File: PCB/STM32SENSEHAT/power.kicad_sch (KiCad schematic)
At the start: 23 parts, among them Q1 FS8205A, U1 MCP1700x-330xxTT, U11 AO3401A_C306862

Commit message: PCB draft
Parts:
- C10, C11, C15, C20, C21: footprint JLCfootprint:C0805 -> Capacitor_SMD:C_0805_2012Metric
- R36, R39, R4, R40, R5, R6: footprint JLCfootprint:R0805 -> Resistor_SMD:R_0805_2012Metric
- U2: value ~ -> DW01A
- U7: value ~ -> TP4056
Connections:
- net BATT+: now also D1.2 (A); no longer BT2.1 (+)
- net at C15.2, Q1.2, Q1.3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: now also BT2.2 (-); no longer D1.1 (K)
- new net: BT2.1 (+), D1.1 (K)
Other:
- moved on the sheet: BT2, R39

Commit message: Changed the footprint of cpacitors C10 and C11 to C_disc"
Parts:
- C10, C11: footprint Capacitor_SMD:C_0805_2012Metric -> Capacitor_THT:C_Disc_D5.0mm_W2.5mm_P5.00mm
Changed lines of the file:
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@@
       (effects (font (size 1.27 1.27)) (justify left))
     )
-    (property "Footprint" "Capacitor_SMD:C_0805_2012Metric" (at 300.99 124.46 0)
+    (property "Footprint" "Capacitor_THT:C_Disc_D5.0mm_W2.5mm_P5.00mm" (at 300.99 124.46 0)
       (effects (font (size 1.27 1.27)) hide)
     )
@@
       (effects (font (size 1.27 1.27)) (justify left))
     )
-    (property "Footprint" "Capacitor_SMD:C_0805_2012Metric" (at 271.78 121.92 0)
-      (effects (font (size 1.27 1.27)) hide)
-    )
+    (property "Footprint" "Capacitor_THT:C_Disc_D5.0mm_W2.5mm_P5.00mm" (at 271.78 121.92 0)
+      (effects (font (size 1.27 1.27)) hide)
+    )

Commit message: Update
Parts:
- C15: value 10nF -> 100nF
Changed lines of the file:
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@@
       (effects (font (size 1.27 1.27)) (justify left))
     )
-    (property "Value" "10nF" (at 107.95 165.7413 0)
+    (property "Value" "100nF" (at 107.95 165.7413 0)
       (effects (font (size 1.27 1.27)) (justify left))
     )

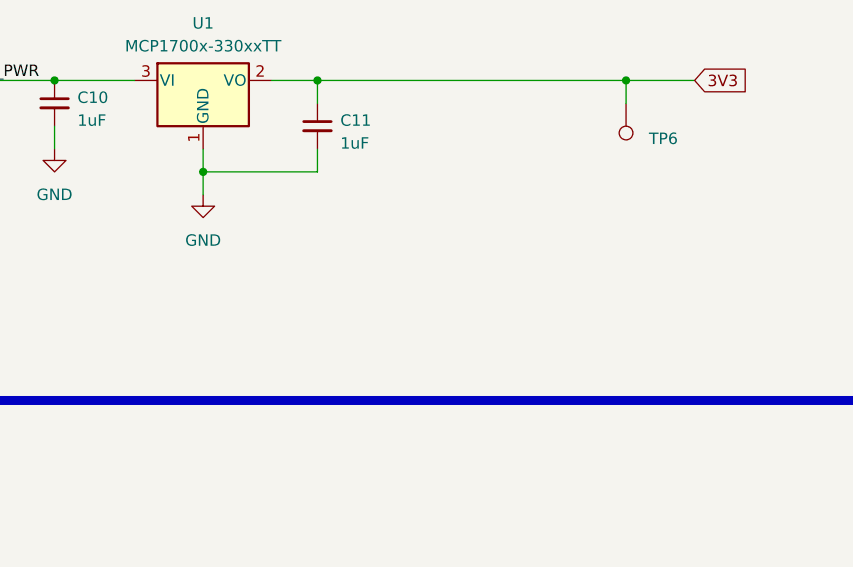
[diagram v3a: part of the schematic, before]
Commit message: Added a poer indicator LED and rectified NRST parastic capacitance
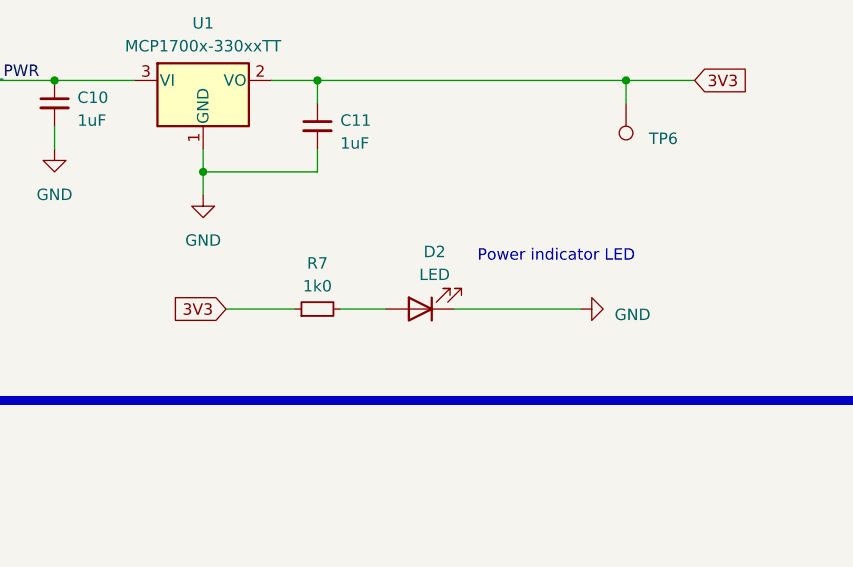
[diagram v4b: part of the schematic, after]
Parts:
- added D2: LED, LED_THT:LED_D5.0mm, symbol Device:LED
- added R7: 1k0, Resistor_SMD:R_0805_2012Metric, symbol Device:R_Small
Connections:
- net 3V3: now also R7.1
- net GND: now also D2.1 (K)
- new net: D2.2 (A), R7.2
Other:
- note added: "Power indicator LED"
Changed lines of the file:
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@@
+    (stroke (width 0) (type default))
+  )
+  (wire (pts (xy 316.23 144.78) (xy 330.2 144.78))
     (stroke (width 0) (type default))
   )
@@
     (stroke (width 0) (type default))
   )
+  (wire (pts (xy 290.83 144.78) (xy 298.45 144.78))
+    (stroke (width 0) (type default))
+  )
   (wire (pts (xy 144.78 92.71) (xy 203.2 92.71))
     (stroke (width 0) (type default))
@@
   )
   (wire (pts (xy 88.9 177.8) (xy 86.36 177.8))
+    (stroke (width 0) (type default))
+  )
+  (wire (pts (xy 303.53 144.78) (xy 308.61 144.78))
     (stroke (width 0) (type default))
   )
@@
     (effects (font (size 5 5) (thickness 0.5) bold) (justify left bottom))
   )
+  (text "Power indicator LED" (at 318.77 139.7 0)
+    (effects (font (size 1.27 1.27)) (justify left bottom))
+  )
   (text "BATTERY PROTECTION" (at 92.71 127 0)
     (effects (font (size 5 5) (thickness 0.5) bold) (justify left bottom))
@@
     )
   )
+  (global_label "3V3" (shape input) (at 290.83 144.78 180) (fields_autoplaced)
+    (effects (font (size 1.27 1.27)) (justify right))
+    (property "Intersheetrefs" "${INTERSHEET_REFS}" (at 284.4166 144.78 0)
+      (effects (font (size 1.27 1.27)) (justify right) hide)
+    )
+  )
   (global_label "5VUSB" (shape input) (at 152.4 139.7 90) (fields_autoplaced)
     (effects (font (size 1.27 1.27)) (justify left))
@@
     )
   )
+  (symbol (lib_id "Device:LED") (at 312.42 144.78 180) (unit 1)
+    (in_bom yes) (on_board yes) (dnp no) (fields_autoplaced)
+    (property "Reference" "D2" (at 314.0075 138.43 0)
+      (effects (font (size 1.27 1.27)))
+    )
+    (property "Value" "LED" (at 314.0075 140.97 0)
+      (effects (font (size 1.27 1.27)))
+    )
+    (property "Footprint" "LED_THT:LED_D5.0mm" (at 312.42 144.78 0)
+      (effects (font (size 1.27 1.27)) hide)
+    )
+    (property "Datasheet" "~" (at 312.42 144.78 0)
+      (effects (font (size 1.27 1.27)) hide)
+    )
+    (property "Basic" "" (at 312.42 144.78 0)
+      (effects (font (size 1.27 1.27)) hide)
+    )
+    (property "DNP" "" (at 312.42 144.78 0)
+      (effects (font (size 1.27 1.27)) hide)
+    )
+    (property "Extended" "" (at 312.42 144.78 0)
+      (effects (font (size 1.27 1.27)) hide)
+    )
+    (property "MOQ and Attrition" "" (at 312.42 144.78 0)
+      (effects (font (size 1.27 1.27)) hide)
+    )
+    (property "Price" "" (at 312.42 144.78 0)
+      (effects (font (size 1.27 1.27)) hide)
+    )
+    (pin "1")
+    (pin "2")
+    (instances
+      (project "STM32SENSEHAT"
+        (path "/e47212d5-bd6f-4bb8-9ec7-12aac08f34b5/e2c75964-4e94-4a3b-9ddf-38bb01f2971b"
+          (reference "D2") (unit 1)
+        )
+      )
+    )
+  )
   (symbol (lib_id "power:GND") (at 166.37 77.47 0) (unit 1)
     (in_bom yes) (on_board yes) (dnp no) (fields_autoplaced)
@@
         (path "/e47212d5-bd6f-4bb8-9ec7-12aac08f34b5/e2c75964-4e94-4a3b-9ddf-38bb01f2971b"
           (reference "R5") (unit 1)
+        )
+      )
+    )
+  )
+  (symbol (lib_id "Device:R_Small") (at 300.99 144.78 90) (unit 1)
+    (in_bom yes) (on_board yes) (dnp no) (fields_autoplaced)
+    (property "Reference" "R7" (at 300.99 139.7 90)
+      (effects (font (size 1.27 1.27)))
+    )
+    (property "Value" "1k0" (at 300.99 142.24 90)
+      (effects (font (size 1.27 1.27)))
+    )
+    (property "Footprint" "Resistor_SMD:R_0805_2012Metric" (at 300.99 144.78 0)
+      (effects (font (size 1.27 1.27)) hide)
+    )
+    (property "Datasheet" "~" (at 300.99 144.78 0)
+      (effects (font (size 1.27 1.27)) hide)
+    )
+    (property "Basic" "" (at 300.99 144.78 0)
+      (effects (font (size 1.27 1.27)) hide)
+    )
+    (property "DNP" "" (at 300.99 144.78 0)
+      (effects (font (size 1.27 1.27)) hide)
+    )
+    (property "Extended" "" (at 300.99 144.78 0)
+      (effects (font (size 1.27 1.27)) hide)
+    )
+    (property "MOQ and Attrition" "" (at 300.99 144.78 0)
+      (effects (font (size 1.27 1.27)) hide)
+    )
+    (property "Price" "" (at 300.99 144.78 0)
+      (effects (font (size 1.27 1.27)) hide)
+    )
+    (pin "1")
+    (pin "2")
+    (instances
+      (project "STM32SENSEHAT"
+        (path "/e47212d5-bd6f-4bb8-9ec7-12aac08f34b5/e2c75964-4e94-4a3b-9ddf-38bb01f2971b"
+          (reference "R7") (unit 1)
         )
       )
@@
         )
       )
+    )
+  )
+  (symbol (lib_id "power:GND") (at 330.2 144.78 90) (unit 1)
+    (in_bom yes) (on_board yes) (dnp no) (fields_autoplaced)
+    (property "Reference" "#PWR039" (at 336.55 144.78 0)
+      (effects (font (size 1.27 1.27)) hide)
+    )
+    (property "Value" "GND" (at 334.01 145.415 90)
+      (effects (font (size 1.27 1.27)) (justify right))
+    )
+    (property "Footprint" "" (at 330.2 144.78 0)
+      (effects (font (size 1.27 1.27)) hide)
+    )
+    (property "Datasheet" "" (at 330.2 144.78 0)
+      (effects (font (size 1.27 1.27)) hide)
+    )
+    (pin "1")
+    (instances
+      (project "STM32SENSEHAT"
+        (path "/e47212d5-bd6f-4bb8-9ec7-12aac08f34b5/e2c75964-4e94-4a3b-9ddf-38bb01f2971b"
+          (reference "#PWR039") (unit 1)
+        )
+      )

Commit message: Added Justin's Feedback
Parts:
- added R22: 1k0, Resistor_SMD:R_0805_2012Metric, symbol Device:R_Small
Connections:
- net 5VUSB: now also R22.1
- net at D4.2 (A), R40.2: no longer D5.2 (A)
- new net: D5.2 (A), R22.2
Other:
- moved on the sheet: D5, R40
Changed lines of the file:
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@@
   (junction (at 128.27 158.75) (diameter 0) (color 0 0 0 0)
   )
-  (junction (at 83.82 49.53) (diameter 0) (color 0 0 0 0)
-  )
   (junction (at 110.49 158.75) (diameter 0) (color 0 0 0 0)
   )
   (junction (at 67.31 191.77) (diameter 0) (color 0 0 0 0)
   )
+  (junction (at 74.93 49.53) (diameter 0) (color 0 0 0 0)
+  )
   (junction (at 165.1 144.78) (diameter 0) (color 0 0 0 0)
   )
@@
   (junction (at 152.4 144.78) (diameter 0) (color 0 0 0 0)
   )
-  (junction (at 83.82 55.88) (diameter 0) (color 0 0 0 0)
-  )
   (junction (at 144.78 92.71) (diameter 0) (color 0 0 0 0)
   )
@@
   )
   (junction (at 173.99 158.75) (diameter 0) (color 0 0 0 0)
+  )
+  (junction (at 88.9 49.53) (diameter 0) (color 0 0 0 0)
   )
   (junction (at 48.26 49.53) (diameter 0) (color 0 0 0 0)
@@
     (stroke (width 0) (type default))
   )
-  (wire (pts (xy 93.98 57.15) (xy 93.98 55.88))
+  (wire (pts (xy 88.9 57.15) (xy 88.9 55.88))
     (stroke (width 0) (type default))
   )
@@
     (stroke (width 0) (type default))
   )
-  (wire (pts (xy 83.82 55.88) (xy 74.93 55.88))
-    (stroke (width 0) (type default))
-  )
   (wire (pts (xy 335.28 119.38) (xy 335.28 121.92))
     (stroke (width 0) (type default))
@@
     (stroke (width 0) (type default))
   )
-  (wire (pts (xy 83.82 49.53) (xy 100.33 49.53))
-    (stroke (width 0) (type default))
-  )
   (wire (pts (xy 132.08 92.71) (xy 144.78 92.71))
     (stroke (width 0) (type default))
@@
     (stroke (width 0) (type default))
   )
+  (wire (pts (xy 74.93 49.53) (xy 88.9 49.53))
+    (stroke (width 0) (type default))
+  )
   (wire (pts (xy 271.78 127) (xy 271.78 124.46))
     (stroke (width 0) (type default))
@@
     (stroke (width 0) (type default))
   )
-  (wire (pts (xy 83.82 49.53) (xy 83.82 50.8))
+  (wire (pts (xy 74.93 49.53) (xy 74.93 50.8))
     (stroke (width 0) (type default))
   )
@@
     (stroke (width 0) (type default))
   )
-  (wire (pts (xy 93.98 55.88) (xy 83.82 55.88))
-    (stroke (width 0) (type default))
-  )
   (wire (pts (xy 128.27 184.15) (xy 128.27 191.77))
     (stroke (width 0) (type default))
@@
     (stroke (width 0) (type default))
   )
+  (wire (pts (xy 88.9 49.53) (xy 88.9 50.8))
+    (stroke (width 0) (type default))
+  )
   (wire (pts (xy 67.31 168.91) (xy 67.31 171.45))
     (stroke (width 0) (type default))
@@
     (stroke (width 0) (type default))
   )
-  (wire (pts (xy 93.98 64.77) (xy 93.98 66.04))
+  (wire (pts (xy 88.9 64.77) (xy 88.9 66.04))
     (stroke (width 0) (type default))
   )
@@
     (stroke (width 0) (type default))
   )
-  (wire (pts (xy 52.07 49.53) (xy 83.82 49.53))
+  (wire (pts (xy 52.07 49.53) (xy 74.93 49.53))
     (stroke (width 0) (type default))
   )
@@
     (stroke (width 0) (type default))
   )
-  (wire (pts (xy 93.98 66.04) (xy 107.95 66.04))
+  (wire (pts (xy 88.9 66.04) (xy 107.95 66.04))
     (stroke (width 0) (type default))
   )
   (wire (pts (xy 110.49 168.91) (xy 110.49 166.37))
+    (stroke (width 0) (type default))
+  )
+  (wire (pts (xy 88.9 49.53) (xy 100.33 49.53))
     (stroke (width 0) (type default))
   )
@@
     )
   )
+  (symbol (lib_id "Device:R_Small") (at 88.9 53.34 0) (unit 1)
+    (in_bom yes) (on_board yes) (dnp no) (fields_autoplaced)
+    (property "Reference" "R22" (at 91.44 52.705 0)
+      (effects (font (size 1.27 1.27)) (justify left))
+    )
+    (property "Value" "1k0" (at 91.44 55.245 0)
+      (effects (font (size 1.27 1.27)) (justify left))
+    )
+    (property "Footprint" "Resistor_SMD:R_0805_2012Metric" (at 88.9 53.34 0)
+      (effects (font (size 1.27 1.27)) hide)
+    )
+    (property "Datasheet" "~" (at 88.9 53.34 0)
+      (effects (font (size 1.27 1.27)) hide)
+    )
+    (property "Basic" "" (at 88.9 53.34 0)
+      (effects (font (size 1.27 1.27)) hide)
+    )
+    (property "DNP" "" (at 88.9 53.34 0)
+      (effects (font (size 1.27 1.27)) hide)
+    )
+    (property "Extended" "" (at 88.9 53.34 0)
+      (effects (font (size 1.27 1.27)) hide)
+    )
+    (property "MOQ and Attrition" "" (at 88.9 53.34 0)
+      (effects (font (size 1.27 1.27)) hide)
+    )
+    (property "Price" "" (at 88.9 53.34 0)
+      (effects (font (size 1.27 1.27)) hide)
+    )
+    (pin "1")
+    (pin "2")
+    (instances
+      (project "STM32SENSEHAT"
+        (path "/e47212d5-bd6f-4bb8-9ec7-12aac08f34b5/e2c75964-4e94-4a3b-9ddf-38bb01f2971b"
+          (reference "R22") (unit 1)
+        )
+      )
+    )
+  )
   (symbol (lib_id "Device:R_Small") (at 152.4 166.37 0) (unit 1)
     (in_bom yes) (on_board yes) (dnp no)
@@
     )
   )
-  (symbol (lib_id "Device:R_Small") (at 83.82 53.34 0) (unit 1)
+  (symbol (lib_id "Device:R_Small") (at 74.93 53.34 0) (unit 1)
     (in_bom yes) (on_board yes) (dnp no) (fields_autoplaced)
-    (property "Reference" "R40" (at 86.36 52.705 0)
+    (property "Reference" "R40" (at 77.47 52.705 0)
       (effects (font (size 1.27 1.27)) (justify left))
     )
-    (property "Value" "1k0" (at 86.36 55.245 0)
+    (property "Value" "1k0" (at 77.47 55.245 0)
       (effects (font (size 1.27 1.27)) (justify left))
     )
-    (property "Footprint" "Resistor_SMD:R_0805_2012Metric" (at 83.82 53.34 0)
-      (effects (font (size 1.27 1.27)) hide)
-    )
-    (property "Datasheet" "~" (at 83.82 53.34 0)
-      (effects (font (size 1.27 1.27)) hide)
-    )
-    (property "Basic" "" (at 83.82 53.34 0)
-      (effects (font (size 1.27 1.27)) hide)
-    )
-    (property "DNP" "" (at 83.82 53.34 0)
-      (effects (font (size 1.27 1.27)) hide)
-    )
-    (property "Extended" "" (at 83.82 53.34 0)
-      (effects (font (size 1.27 1.27)) hide)
-    )
-    (property "MOQ and Attrition" "" (at 83.82 53.34 0)
-      (effects (font (size 1.27 1.27)) hide)
-    )
-    (property "Price" "" (at 83.82 53.34 0)
+    (property "Footprint" "Resistor_SMD:R_0805_2012Metric" (at 74.93 53.34 0)
+      (effects (font (size 1.27 1.27)) hide)
+    )
+    (property "Datasheet" "~" (at 74.93 53.34 0)
+      (effects (font (size 1.27 1.27)) hide)
+    )
+    (property "Basic" "" (at 74.93 53.34 0)
+      (effects (font (size 1.27 1.27)) hide)
+    )
+    (property "DNP" "" (at 74.93 53.34 0)
+      (effects (font (size 1.27 1.27)) hide)
+    )
+    (property "Extended" "" (at 74.93 53.34 0)
+      (effects (font (size 1.27 1.27)) hide)
+    )
+    (property "MOQ and Attrition" "" (at 74.93 53.34 0)
+      (effects (font (size 1.27 1.27)) hide)
+    )
+    (property "Price" "" (at 74.93 53.34 0)
       (effects (font (size 1.27 1.27)) hide)
     )
@@
     )
   )
-  (symbol (lib_id "Device:LED") (at 93.98 60.96 90) (unit 1)
+  (symbol (lib_id "Device:LED") (at 88.9 60.96 90) (unit 1)
     (in_bom yes) (on_board yes) (dnp no) (fields_autoplaced)
-    (property "Reference" "D5" (at 97.79 61.9125 90)
+    (property "Reference" "D5" (at 92.71 61.9125 90)
       (effects (font (size 1.27 1.27)) (justify right))
     )
-    (property "Value" "LED" (at 97.79 64.4525 90)
+    (property "Value" "LED" (at 92.71 64.4525 90)
       (effects (font (size 1.27 1.27)) (justify right))
     )
-    (property "Footprint" "LED_THT:LED_D5.0mm" (at 93.98 60.96 0)
-      (effects (font (size 1.27 1.27)) hide)
-    )
-    (property "Datasheet" "~" (at 93.98 60.96 0)
-      (effects (font (size 1.27 1.27)) hide)
-    )
-    (property "Basic" "" (at 93.98 60.96 0)
-      (effects (font (size 1.27 1.27)) hide)
-    )
-    (property "DNP" "" (at 93.98 60.96 0)
-      (effects (font (size 1.27 1.27)) hide)
-    )
-    (property "Extended" "" (at 93.98 60.96 0)
-      (effects (font (size 1.27 1.27)) hide)
-    )
-    (property "MOQ and Attrition" "" (at 93.98 60.96 0)
-      (effects (font (size 1.27 1.27)) hide)
-    )
-    (property "Price" "" (at 93.98 60.96 0)
-      (effects (font (size 1.27 1.27)) hide)
-    )
+    (property "Footprint" "LED_THT:LED_D5.0mm" (at 88.9 60.96 0)
+      (effects (font (size 1.27 1.27)) hide)
+    )
+    (property "Datasheet" "~" (at 88.9 60.96 0)
+      (effects (font (size 1.27 1.27)) hide)
+    )
+    (property "Basic" "" (at 88.9 60.96 0)
+      (effects (font (size 1.27 1.27)) hide)
+    )
+    (property "DNP" "" (at 88.9 60.96 0)
+      (effects (font (size 1.27 1.27)) hide)
+    )
+    (property "Extended" "" (at 88.9 60.96 0)
+      (effects (font (size 1.27 1.27)) hide)
+    )
+    (property "MOQ and Attrition" "" (at 88.9 60.96 0)
+      (effects (font (size 1.27 1.27)) hide)
+    )
+    (property "Price" "" (at 88.9 60.96 0)
+      (effects (font (size 1.27 1.27)) hide)
+    )

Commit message: Last change
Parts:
- removed C20, C21: 10uF, Capacitor_SMD:C_0805_2012Metric, symbol Device:C_Small
- removed D4, D5: LED, LED_THT:LED_D5.0mm, symbol Device:LED
- removed D6: D_Schottky, JLCfootprint:SOT-23-3_L3.0-W1.7-P0.95-LS2.9-BR, symbol Device:D_Schottky
- removed R22, R40: 1k0, Resistor_SMD:R_0805_2012Metric, symbol Device:R_Small
- removed R36: 10k, Resistor_SMD:R_0805_2012Metric, symbol Device:R_Small
- removed R39: 0R, Resistor_SMD:R_0805_2012Metric, symbol Device:R_Small
- removed TP5: TestPoint, TestPoint:TestPoint_Pad_D3.0mm, symbol Connector:TestPoint
- removed U7: TP4056, JLCfootprint:ESOP-8_L4.9-W3.9-P1.27-LS6.0-BL-EP, symbol UCT:TP4056
- added C22, C23: 4.7uF, Capacitor_SMD:C_0805_2012Metric, symbol Device:C_Small
- added D3: LED, LED_THT:LED_D5.0mm, symbol Device:LED
- added Q2: IRF9520, TO254P1052X465X1989-3, symbol IRF9520:IRF9520
- added R23, R24, R25: 1k0, Resistor_SMD:R_0805_2012Metric, symbol Device:R_Small
- added R26, R27: 2k0, Resistor_SMD:R_0805_2012Metric, symbol Device:R_Small
- added U10: TL431D, Package_SO:SOIC-8_3.9x4.9mm_P1.27mm, symbol Reference_Voltage:TL431D
- added U12: MCP73831-2-OT, Package_TO_SOT_SMD:SOT-23-5, symbol Battery_Management:MCP73831-2-OT
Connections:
- net 5VUSB: now also D1.2 (A), C22.1, D3.2 (A), U12.4 (V_{DD})
- net BATT+: now also BT2.1 (+), C23.1, Q2.3, R23.1, R25.1, U12.3 (V_{BAT}); no longer D1.2 (A), U11.3 (D)
- net GND: now also BT2.2 (-), C15.2, Q1.2, Q1.3, U2.6 (GND), C22.2, C23.2, R24.2, R26.1, U10.2 (A), U10.3 (A), U10.6 (A), U10.7 (A), U12.2 (V_{SS})
- net LOAD_PWR: now also D1.1 (K)
- new net: R27.1, U12.1 (STAT)
- new net: D3.1 (K), R27.2
- new net: Q2.1, R25.2, U10.1 (K)
- new net: Q2.2, U11.3 (D)
- new net: R23.2, R24.1, U10.8 (REF)
- new net: R26.2, U12.5 (PROG)
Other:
- note added: "Calculate threshold for cutoff, Vth = 2.5(R1/R2 +1)"
- moved on the sheet: C10, C11, D2, R7, TP6, U1
